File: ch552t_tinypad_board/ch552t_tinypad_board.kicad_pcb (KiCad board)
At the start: 2 copper layers, 91 x 55 mm, 19 parts, among them J1 Conn_02x10_Odd_Even, J2 Conn_01x02_Pin, J3 USB_C_Receptacle_USB2.0, SW1 SW_Push, SW2 SW_Push, SW3 SW_Push, SW4 SW_Push, SW5 SW_Push, SW6 SW_Push, U1 CH552T

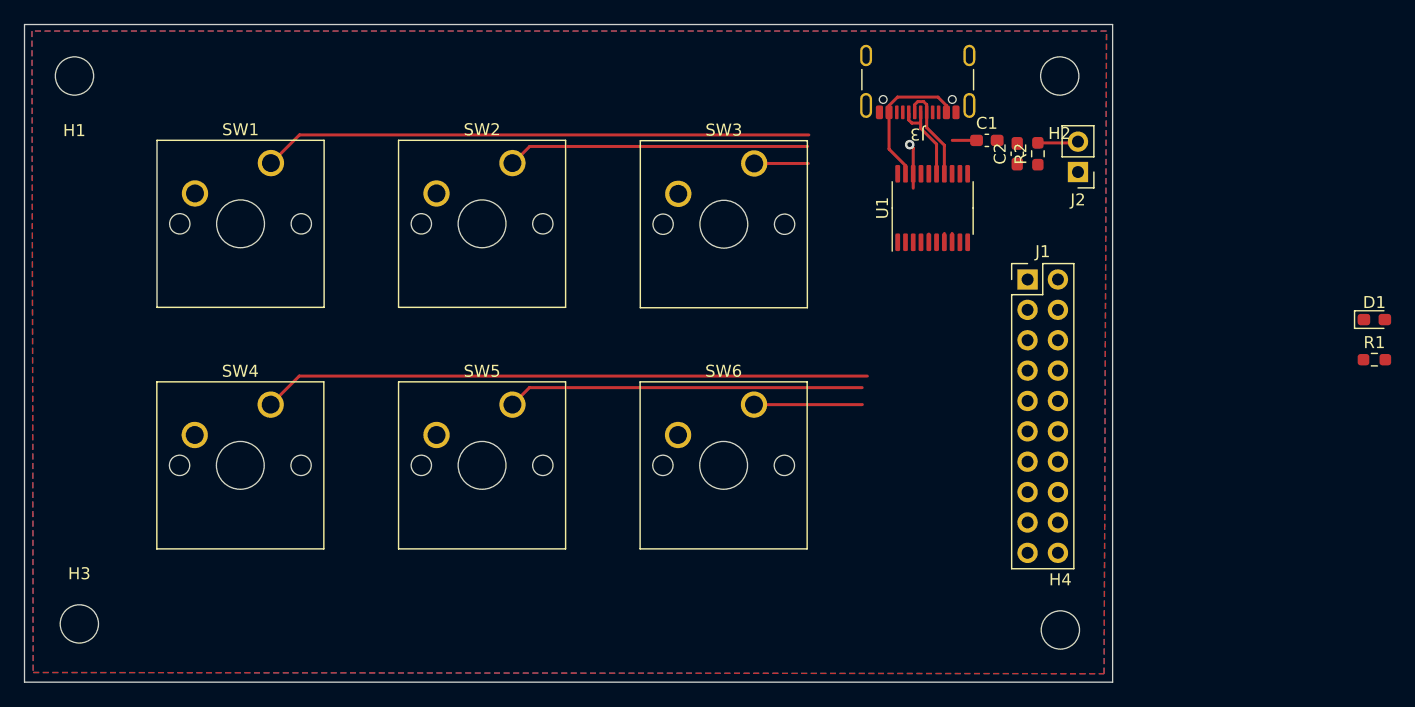
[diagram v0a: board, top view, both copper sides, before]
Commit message: feat: auto wiring and board outline
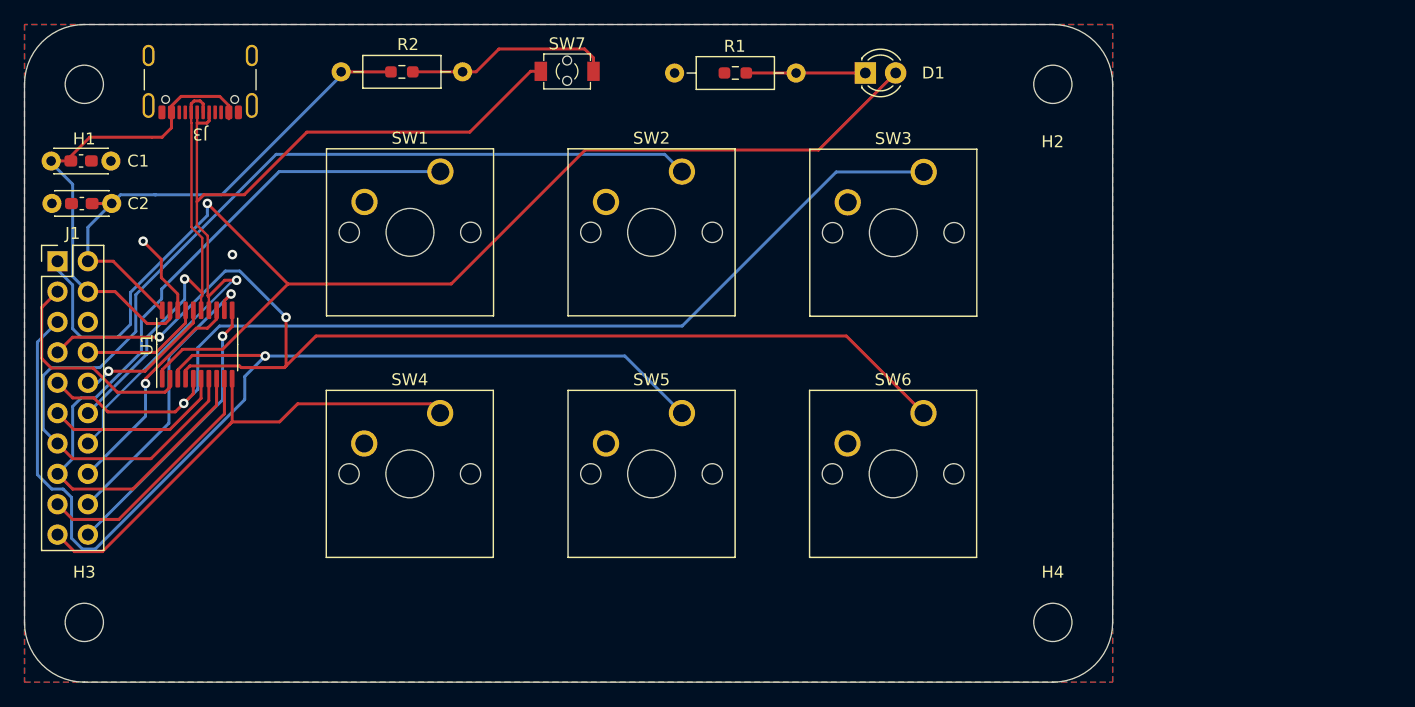
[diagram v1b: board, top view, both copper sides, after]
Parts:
- removed J2: Conn_01x02_Pin, Connector_PinHeader_2.54mm:PinHeader_1x02_P2.54mm_Vertical
- added SW7: SW_Push, Library:SW_SPST_TVAF06_A020B_R, F.Cu at (84.4, 34.9)
- C1, C2: footprint Capacitor_SMD:C_0603_1608Metric_Pad1.08x0.95mm_HandSolder -> Library:C_SMD_0603_1608_Disc_DualUse
- D1: footprint LED_SMD:LED_0603_1608Metric_Pad1.05x0.95mm_HandSolder -> LED_THT:LED_D3.0mm
- R1, R2: footprint Resistor_SMD:R_0603_1608Metric_Pad0.98x0.95mm_HandSolder -> Library:R_SMD_0603_1608_THT_DIN0207_DualUse
- moved J1 81.1 mm to (41.8, 50.8)
- moved C1 78.3 mm to (41.2, 42.4)
- moved C2 75.8 mm to (46.3, 46.0), turned to 180 degrees
- moved U1 62.6 mm to (53.4, 57.8)
- moved J3 60.0 mm to (53.7, 34.7)
- moved R2 58.7 mm to (65.5, 35.0), turned to 0 degrees
- moved R1 54.0 mm to (103.5, 35.1), turned to 180 degrees
- moved D1 47.3 mm to (109.3, 35.1)
- moved SW2 14.2 mm to (94.0, 43.3)
- moved SW3 14.2 mm to (114.2, 43.3)
- moved SW5 14.2 mm to (94.0, 63.5)
- moved SW6 14.2 mm to (114.2, 63.5)
- moved SW1 14.2 mm to (73.8, 43.3)
- moved SW4 14.2 mm to (73.8, 63.5)
- moved H1 1.07 mm to (44.0, 36.0)
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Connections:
- net /P3.6 renamed /D+
- net /P3.7 renamed /D-
- SW4 pad 1: /P1.4 -> /P3.0
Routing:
- net /P3.2: track 0.00 -> 106.4 mm, vias 0 -> 1
- net /P1.6: track 9.06 -> 94.0 mm, vias 0 -> 2
- net /P1.7: track 5.21 -> 86.2 mm, vias 0 -> 1
- net /D+: track 8.26 -> 74.3 mm, vias 0 -> 1
- net /P1.0: track 26.0 -> 86.7 mm
- net /P1.5: track 29.8 -> 90.3 mm, vias 0 -> 1
- net /3V3: track 0.00 -> 43.4 mm
- net /P3.0: track 0.00 -> 41.6 mm
- net /P1.4: track 50.9 -> 18.9 mm
- net /D-: track 7.47 -> 36.1 mm, vias 0 -> 1
- net VCC: track 14.3 -> 40.9 mm
- net /P3.4: track 0.00 -> 24.1 mm, vias 0 -> 1
- net /P3.3: track 0.00 -> 23.8 mm, vias 0 -> 1
- net /P3.1: track 0.00 -> 21.1 mm
- net /P1.1: track 46.7 -> 66.1 mm
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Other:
- outline, holes or cut-outs redrawn

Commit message: feat: connect keys to MCU
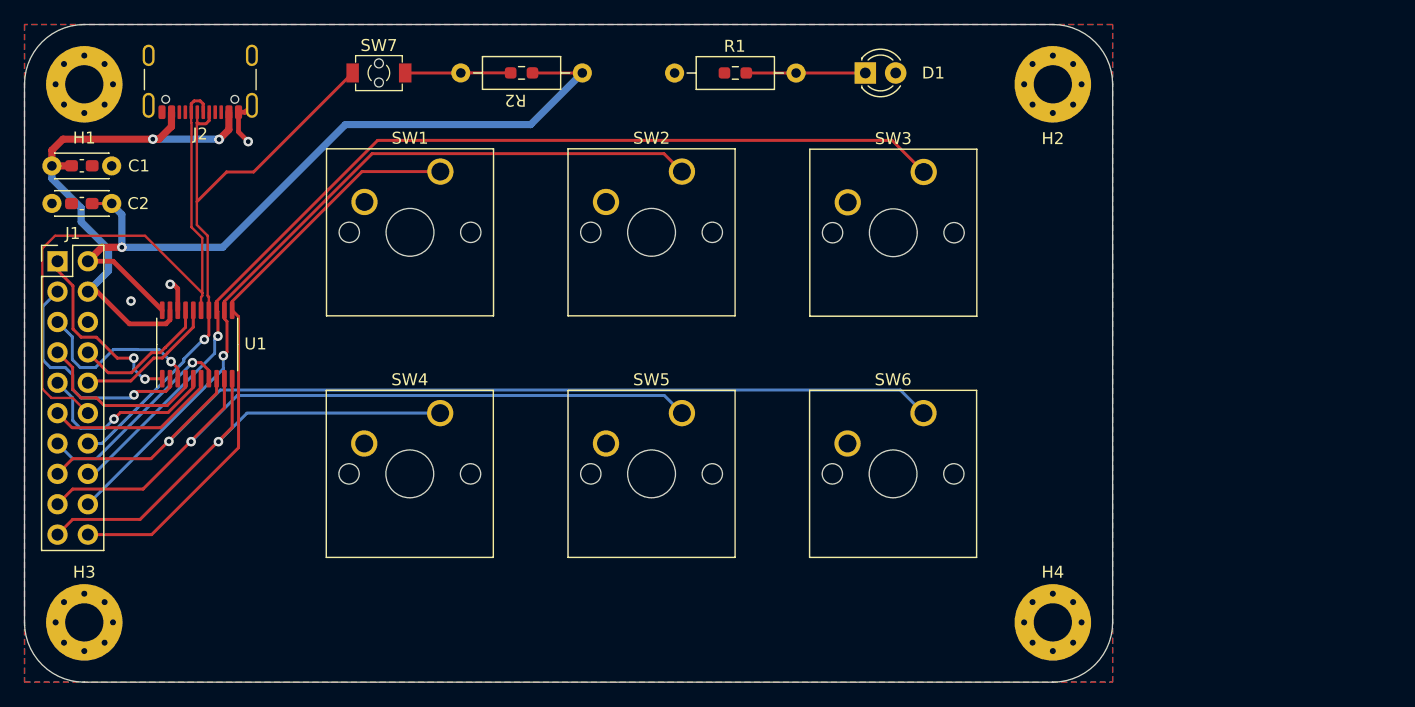
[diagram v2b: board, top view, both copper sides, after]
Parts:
- removed J3: USB_C_Receptacle_USB2.0, Connector_USB:USB_C_Receptacle_GCT_USB4105-xx-A_16P_TopMnt_Horizontal
- added J2: USB_C_Receptacle_USB2.0, Connector_USB:USB_C_Receptacle_GCT_USB4105-xx-A_16P_TopMnt_Horizontal, F.Cu at (53.7, 34.7)
- H1, H2, H3, H4: value MountingHole -> MountingHole_Pad; footprint MountingHole:MountingHole_3.2mm_M3 -> MountingHole:MountingHole_3.2mm_M3_Pad_Via
- moved R2 20.2 mm to (85.6, 35.1), turned to 180 degrees
- moved SW7 15.7 mm to (68.6, 35.1)
- moved C1 0.41 mm to (41.3, 42.8)
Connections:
- D1 pad 2: /P3.2 -> unconnected-(D1-A-Pad2)
- SW1 pad 1: /P1.1 -> /P3.3
- SW2 pad 1: /P1.0 -> /P3.4
- SW3 pad 1: /P1.7 -> /P3.5
- SW5 pad 1: /P1.5 -> /P3.1
- SW6 pad 1: /P1.6 -> /P1.1
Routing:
- net /P3.2: track 106.4 -> 16.0 mm, vias 1 -> 2
- net /P1.6: track 94.0 -> 15.0 mm, vias 2 -> 0
- net /P1.5: track 90.3 -> 14.9 mm
- net /P1.7: track 86.2 -> 16.2 mm
- net /P1.0: track 86.7 -> 17.5 mm, vias 0 -> 1
- net /P3.5: track 18.7 -> 85.1 mm
- net /P3.1: track 21.1 -> 63.0 mm, vias 0 -> 1
- net /P3.4: track 24.1 -> 65.9 mm
- net /P3.3: track 23.8 -> 50.0 mm, vias 1 -> 0
- net /3V3: track 43.4 -> 65.6 mm, vias 0 -> 1
- net /D+: track 74.3 -> 52.6 mm
- net /P1.1: track 66.1 -> 83.0 mm, vias 0 -> 1
- net /D-: track 36.1 -> 51.8 mm, vias 1 -> 0
- net Net-(R2-Pad2): track 17.3 -> 8.83 mm
- net VCC: track 40.9 -> 46.0 mm, vias 0 -> 2
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
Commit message: fix: pulldown CC pins on USB-C
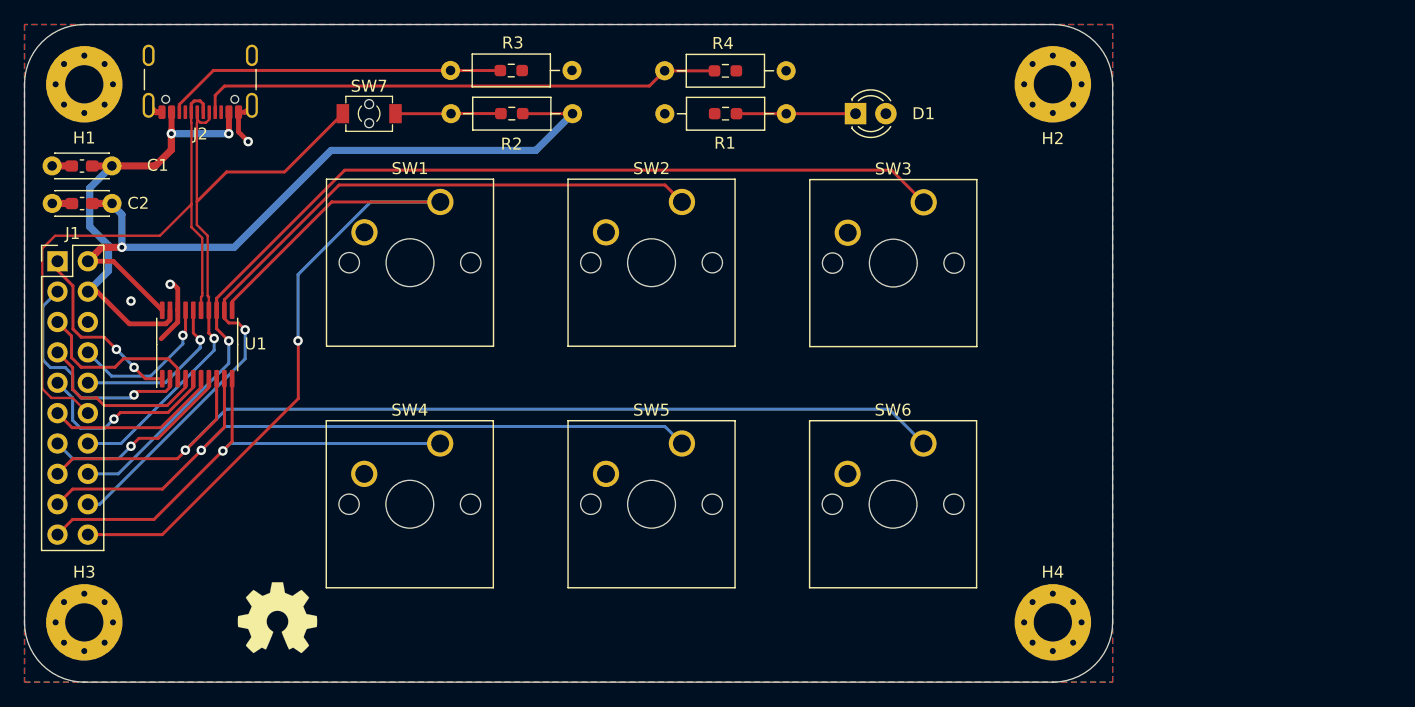
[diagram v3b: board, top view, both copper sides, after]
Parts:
- added G***: LOGO, Library:mcc_logo_full, B.Cu at (69.1, 79.2)
- added R3: R, Library:R_SMD_0603_1608_THT_DIN0207_DualUse, F.Cu at (74.6, 34.8)
- added R4: R, Library:R_SMD_0603_1608_THT_DIN0207_DualUse, F.Cu at (92.5, 34.9)
- added REF**: OSHW-Symbol_6.7x6mm_SilkScreen, Symbol:OSHW-Symbol_6.7x6mm_SilkScreen, F.Cu at (60.1, 80.6)
- moved SW7 3.50 mm to (67.8, 38.5)
- moved D1 3.50 mm to (108.5, 38.5)
- moved R1 3.50 mm to (102.7, 38.5)
- moved R2 3.50 mm to (84.8, 38.5)
- moved SW1 2.54 mm to (73.8, 45.8)
- moved SW2 2.54 mm to (94.0, 45.8)
- moved SW4 2.54 mm to (73.8, 66.0)
- moved SW5 2.54 mm to (94.0, 66.0)
- moved SW6 2.54 mm to (114.2, 66.0)
- moved SW3 2.54 mm to (114.2, 45.9)
- moved C1 2.52 mm to (43.8, 42.8), turned to 180 degrees
- moved C2 2.48 mm to (43.8, 46.0)
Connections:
- J2 pad A5: unconnected-(J2-CC1-PadA5) -> Net-(J2-CC1)
- J2 pad B5: unconnected-(J2-CC2-PadB5) -> Net-(J2-CC2)
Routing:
- net Net-(J2-CC1): track 0.00 -> 44.0 mm
- net Net-(J2-CC2): track 0.00 -> 28.7 mm
- net /P3.3: track 50.0 -> 69.0 mm, vias 0 -> 1
- net VCC: track 46.0 -> 37.8 mm
- net GND: track 6.75 -> 14.3 mm
- net /P1.3: track 12.2 -> 14.2 mm, vias 0 -> 1
- net /P3.4: track 65.9 -> 67.9 mm
- net /P3.5: track 85.1 -> 86.9 mm
- net /D-: track 51.8 -> 50.0 mm
- net /P1.0: track 17.5 -> 16.4 mm
- net /P1.2: track 11.9 -> 12.8 mm, vias 0 -> 1
- net /P1.5: track 14.9 -> 14.2 mm, vias 1 -> 0
- net /P3.1: track 63.0 -> 62.3 mm
- net /3V3: track 65.6 -> 65.0 mm
- net /P3.2: track 16.0 -> 15.4 mm

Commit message: feat: silkscreen artwork(?)
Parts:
- removed the REF** at (60.1, 80.6)
- added G***: LOGO, Library:mcc_logo, F.Cu at (59.3, 79.2)
- added G***: LOGO, Library:github_logo, B.Cu at (117.4, 82.5)
- added G***: LOGO, Library:twitter_x_logo, B.Cu at (114.4, 82.5)
- added REF**: OSHW-Logo2_7.3x6mm_SilkScreen, Symbol:OSHW-Logo2_7.3x6mm_SilkScreen, F.Cu at (52.7, 79.5)
- moved G*** 2.52 mm to (66.5, 79.4)
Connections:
- D1 pad 2: unconnected-(D1-A-Pad2) -> /P1.0
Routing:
- net /P1.0: track 16.4 -> 93.0 mm
- net GND: track 14.3 -> 17.1 mm
- net VCC: track 37.8 -> 40.0 mm
- net /P3.5: track 86.9 -> 88.7 mm
- net /P3.4: track 67.9 -> 69.4 mm
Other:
- board text added: "@HongoMCC"
- board text added: "https://github.com/HongoMCC/ch552t_tinypad"
- board text added: "|P1.0| |P3.3|P3.4|P3.5| |P3.0|P3.1|P1.1|"
- board text added: "私立本郷中学校・高等学校 マイコン部 電子工作班"

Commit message: feat: add revision number on silkscreen
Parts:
- moved REF** 72.5 mm to (125.0, 73.8)
- moved G*** 66.7 mm to (125.0, 67.7)
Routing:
- net GND: track 17.1 -> 20.6 mm
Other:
- board text added: "CH552T_TinyPad Rev.1 by @ctes091x https://github.com/HongoMCC/ch552t_tinypad"
- board text removed: "https://github.com/HongoMCC/ch552t_tinypad"
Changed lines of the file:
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@@
   (net 26 "Net-(R2-Pad2)")
   (footprint "Symbol:OSHW-Logo2_7.3x6mm_SilkScreen" (layer "F.Cu")
-    (at 52.7214 79.5302)
+    (at 125 73.8)
     (descr "Open Source Hardware Symbol")
     (tags "Logo Symbol OSHW")
@@
     (property "ki_keywords" "mounting hole")
     (attr exclude_from_pos_files)
-    (fp_text reference "H3" (at 0 -4.2) (layer "F.SilkS")
+    (fp_text reference "H3" (at 0 -4.2) (layer "F.SilkS") hide
         (effects (font (size 1 1) (thickness 0.15)))
     )
@@
     (property "ki_keywords" "mounting hole")
     (attr exclude_from_pos_files)
-    (fp_text reference "H1" (at -0.0072 4.4876) (layer "F.SilkS")
+    (fp_text reference "H1" (at -0.0072 4.4876) (layer "F.SilkS") hide
         (effects (font (size 1 1) (thickness 0.15)))
     )
@@
   )
   (footprint "Library:mcc_logo" (layer "F.Cu")
-    (at 59.3 79.2)
+    (at 125 67.7)
     (attr board_only exclude_from_pos_files exclude_from_bom)
     (fp_text reference "G***" (at 0 0) (layer "F.SilkS") hide
@@
   )
   (footprint "Connector_USB:USB_C_Receptacle_GCT_USB4105-xx-A_16P_TopMnt_Horizontal" (layer "F.Cu")
-    (at 53.6976 34.6538 180)
+    (at 53.7 34.61 180)
     (descr "USB 2.0 Type C Receptacle, GCT, 16P, top mounted, horizontal, 5A: https://gct.co/files/drawings/usb4105.pdf")
     (tags "USB C Type-C Receptacle SMD USB 2.0 16P 16C USB4105-15-A USB4105-15-A-060 USB4105-15-A-120 USB4105-GF-A USB4105-GF-A-060 USB4105-GF-A-120")
@@
     (property "ki_keywords" "mounting hole")
     (attr exclude_from_pos_files)
-    (fp_text reference "H2" (at 0 4.5384) (layer "F.SilkS")
+    (fp_text reference "H2" (at 0 4.5384) (layer "F.SilkS") hide
         (effects (font (size 1 1) (thickness 0.15)))
     )
@@
     (property "ki_keywords" "mounting hole")
     (attr exclude_from_pos_files)
-    (fp_text reference "H4" (at 0 -4.2) (layer "F.SilkS")
+    (fp_text reference "H4" (at 0 -4.2) (layer "F.SilkS") hide
         (effects (font (size 1 1) (thickness 0.15)))
     )
@@
     (effects (font (size 1 1) (thickness 0.15)) (justify right bottom))
   )
-  (gr_text "https://github.com/HongoMCC/ch552t_tinypad" (at 49.172102 84.023661) (layer "F.SilkS")
+  (gr_text "CH552T_TinyPad Rev.1 by @ctes091x\nhttps://github.com/HongoMCC/ch552t_tinypad" (at 49.1 84.4) (layer "F.SilkS")
     (effects (font (size 1 1) (thickness 0.15)) (justify left bottom))
   )
@@
     (pts (xy 39 31) (xy 44 31))
     (height 61.5)
-    (gr_text "5.0000 mm" (at 41.5 91.35) (layer "Eco1.User")
+    (gr_text "0.1969 in" (at 41.5 91.35) (layer "Eco1.User")
       (effects (font (size 1 1) (thickness 0.15)))
     )
@@
     (pts (xy 130 31) (xy 125 31))
     (height -61.5)
-    (gr_text "5.0000 mm" (at 127.5 91.35) (layer "Eco1.User")
+    (gr_text "0.1969 in" (at 127.5 91.35) (layer "Eco1.User")
       (effects (font (size 1 1) (thickness 0.15)))
     )
@@
     (pts (xy 130 86) (xy 130 81))
     (height -96.7)
-    (gr_text "5.0000 mm" (at 32.15 83.5 90) (layer "Eco1.User")
+    (gr_text "0.1969 in" (at 32.15 83.5 90) (layer "Eco1.User")
       (effects (font (size 1 1) (thickness 0.15)))
     )
@@
     (pts (xy 130 31) (xy 130 36))
     (height 97.4)
-    (gr_text "5.0000 mm" (at 31.45 33.5 90) (layer "Eco1.User")
+    (gr_text "0.1969 in" (at 31.45 33.5 90) (layer "Eco1.User")
       (effects (font (size 1 1) (thickness 0.15)))
     )
@@
     (pts (xy 130 31) (xy 130 86))
     (height 104.2)
-    (gr_text "55.0000 mm" (at 24.65 58.5 90) (layer "Eco2.User")
+    (gr_text "2.1654 in" (at 24.65 58.5 90) (layer "Eco2.User")
       (effects (font (size 1 1) (thickness 0.15)))
     )
@@
     (pts (xy 39 31) (xy 130 31))
     (height 66.7)
-    (gr_text "91.0000 mm" (at 84.5 96.55) (layer "Eco2.User")
+    (gr_text "3.5827 in" (at 84.5 96.55) (layer "Eco2.User")
       (effects (font (size 1 1) (thickness 0.15)))
     )
@@
   (segment (start 50.4976 38.3338) (end 49.9526 38.3338) (width 0.5) (layer "F.Cu") (net 2))
   (segment (start 50.429836 57.277) (end 51.8166 55.890236) (width 0.4) (layer "F.Cu") (net 2))
+  (segment (start 50.429836 57.277) (end 48.1838 57.277) (width 0.4) (layer "F.Cu") (net 2))
   (segment (start 42.9436 45.964) (end 42.9536 45.974) (width 0.6) (layer "F.Cu") (net 2))
+  (segment (start 48.1838 57.277) (end 47.2948 56.388) (width 0.4) (layer "F.Cu") (net 2))
   (segment (start 56.8976 38.3338) (end 57.4426 38.3338) (width 0.4) (layer "F.Cu") (net 2))
   (segment (start 49.9526 38.3338) (end 49.3776 37.7588) (width 0.5) (layer "F.Cu") (net 2))
